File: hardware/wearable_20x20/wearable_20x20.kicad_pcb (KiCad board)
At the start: 4 copper layers, 49.3 x 49.3 mm, 400 parts

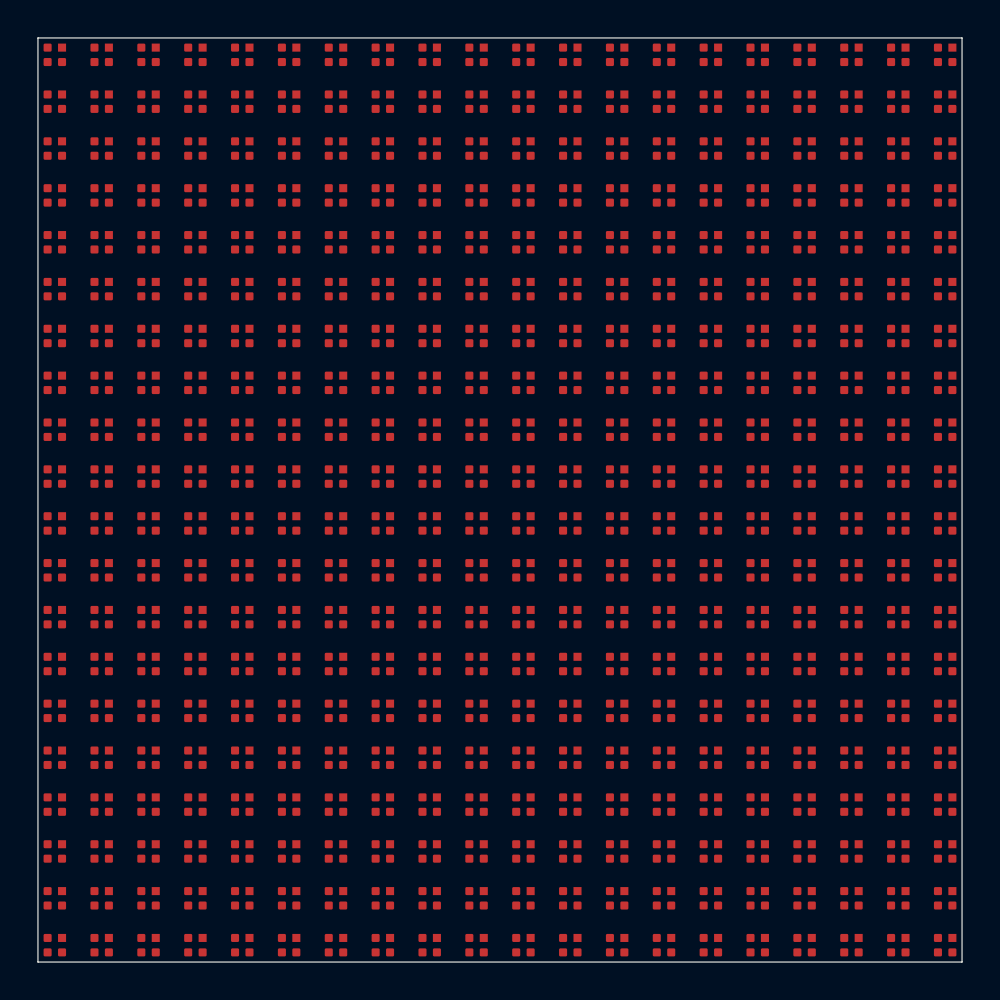
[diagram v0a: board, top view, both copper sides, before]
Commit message: Promote verified matrix routing and release gates
Co-authored-by: illiapliukhin <illiapliukhin@users.noreply.github.com>
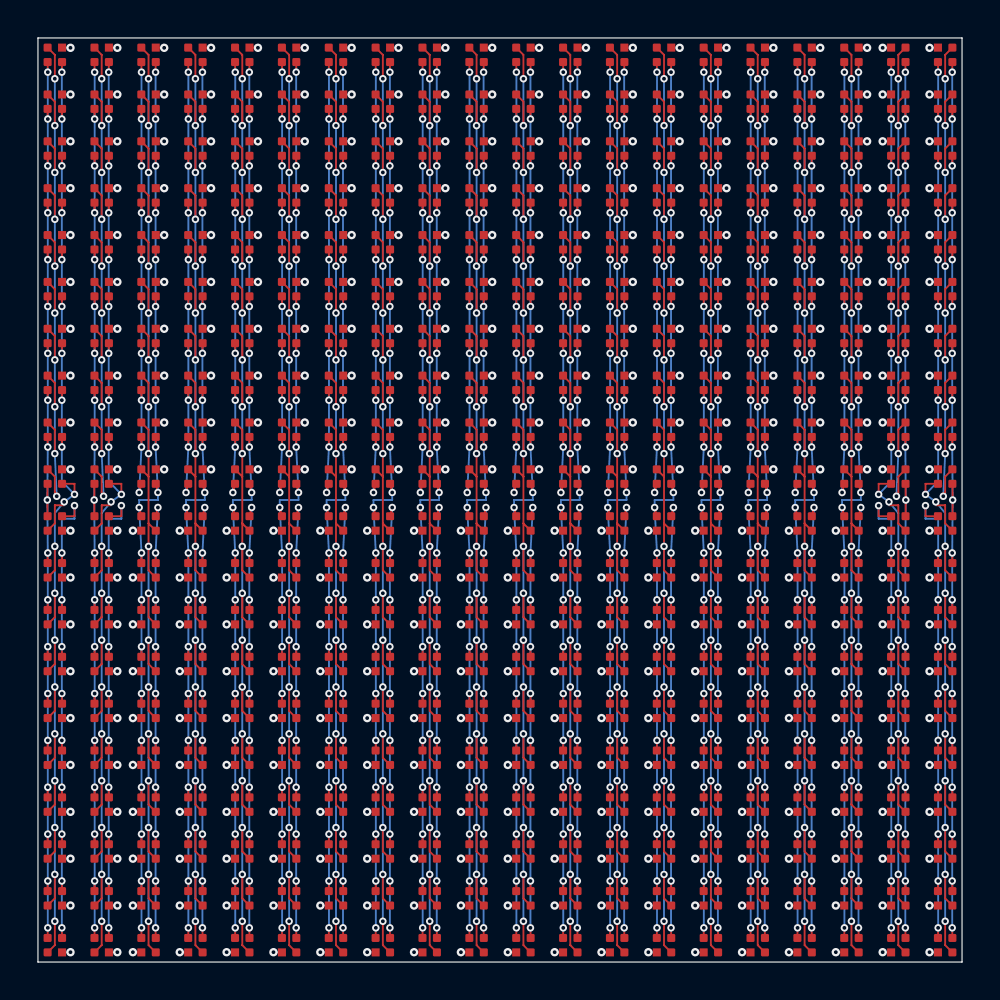
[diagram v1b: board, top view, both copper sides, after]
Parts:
- turned D100 to 90 degrees
- turned D119 to 90 degrees
- turned D120 to 90 degrees
- turned D139 to 90 degrees
- turned D140 to 90 degrees
- turned D159 to 90 degrees
- turned D160 to 90 degrees
- turned D179 to 90 degrees
- turned D180 to 90 degrees
- turned D19 to 90 degrees
- turned D199 to 90 degrees
- turned D20 to 90 degrees
- turned D200 to 90 degrees
- turned D201 to -90 degrees
- turned D202 to -90 degrees
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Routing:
- net COL_B_13: track 0.00 -> 78.8 mm, vias 0 -> 18
- net COL_B_12: track 0.00 -> 78.8 mm, vias 0 -> 18
- net COL_B_11: track 0.00 -> 78.8 mm, vias 0 -> 18
- net COL_B_10: track 0.00 -> 78.8 mm, vias 0 -> 18
- net COL_B_09: track 0.00 -> 78.8 mm, vias 0 -> 18
- net COL_B_08: track 0.00 -> 78.8 mm, vias 0 -> 18
- net COL_B_07: track 0.00 -> 78.8 mm, vias 0 -> 18
- net COL_B_06: track 0.00 -> 78.8 mm, vias 0 -> 18
- net COL_B_05: track 0.00 -> 78.8 mm, vias 0 -> 18
- net COL_B_04: track 0.00 -> 78.8 mm, vias 0 -> 18
- net COL_B_03: track 0.00 -> 78.8 mm, vias 0 -> 18
- net COL_B_18: track 0.00 -> 78.8 mm, vias 0 -> 18
- net COL_B_17: track 0.00 -> 78.8 mm, vias 0 -> 18
- net COL_B_16: track 0.00 -> 78.8 mm, vias 0 -> 18
- net COL_B_15: track 0.00 -> 78.8 mm, vias 0 -> 18
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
